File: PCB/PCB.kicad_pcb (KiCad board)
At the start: 2 copper layers, 60 x 70 mm, 6 parts

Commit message: update pcb
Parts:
- removed MD1, MD2: Conn_01x02_Pin, Connector_PinHeader_2.54mm:PinHeader_1x02_P2.54mm_Vertical
- removed MOTOR1, MOTOR2: Conn_01x09, Connector_PinHeader_2.54mm:PinHeader_1x09_P2.54mm_Vertical
- added D1: LED_RKGB, LED_THT:LED_D5.0mm-4_RGB_Wide_Pins, F.Cu at (86.7, 97.2)
- added J1: Servo_Conn_1, Connector_PinHeader_2.54mm:PinHeader_1x03_P2.54mm_Vertical, F.Cu at (64.5, 66.8)
- added J10: Conn_01x04_Pin, Connector_PinHeader_2.54mm:PinHeader_1x04_P2.54mm_Vertical, F.Cu at (82.8, 83.6)
- added J11: UBEC_Pow_In, Connector_PinHeader_2.54mm:PinHeader_1x02_P2.54mm_Horizontal, F.Cu at (78.2, 76.4)
- added J12: Spare_GPIO_Conn, Connector_PinHeader_2.54mm:PinHeader_1x10_P2.54mm_Vertical, F.Cu at (64.5, 76.4)
- added J2: Servo_Conn_2, Connector_PinHeader_2.54mm:PinHeader_1x03_P2.54mm_Vertical, F.Cu at (69.1, 66.8)
- added J3: Servo_Conn_3, Connector_PinHeader_2.54mm:PinHeader_1x03_P2.54mm_Vertical, F.Cu at (73.6, 66.8)
- added J4: Servo_Conn_4, Connector_PinHeader_2.54mm:PinHeader_1x03_P2.54mm_Vertical, F.Cu at (78.2, 66.8)
- added J5: Servo_Conn_5, Connector_PinHeader_2.54mm:PinHeader_1x03_P2.54mm_Vertical, F.Cu at (82.8, 66.8)
- added J6: Servo_Conn_6, Connector_PinHeader_2.54mm:PinHeader_1x03_P2.54mm_Vertical, F.Cu at (87.4, 66.8)
- added J7: Mot1_Conn, Connector_PinHeader_2.54mm:PinHeader_1x06_P2.54mm_Vertical, F.Cu at (69.1, 76.4)
- added J8: Mot2_Conn, Connector_PinHeader_2.54mm:PinHeader_1x06_P2.54mm_Vertical, F.Cu at (73.6, 76.4)
- added J9: Conn_01x04_Pin, Connector_PinHeader_2.54mm:PinHeader_1x04_P2.54mm_Vertical, F.Cu at (78.2, 83.6)
- added R1: 220R, Resistor_THT:R_Axial_DIN0207_L6.3mm_D2.5mm_P7.62mm_Horizontal, F.Cu at (86.7, 83.3)
- added R2: 220R, Resistor_THT:R_Axial_DIN0207_L6.3mm_D2.5mm_P7.62mm_Horizontal, F.Cu at (86.7, 87.3)
- added R3: 220R, Resistor_THT:R_Axial_DIN0207_L6.3mm_D2.5mm_P7.62mm_Horizontal, F.Cu at (86.7, 91.4)
- renumbered MOTOR_DRIVER1 to MOT_DRV_Conn1
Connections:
- net Net-(A2-GPIO21) renamed /PWM2
- A2 pad 1: unconnected-(A2-GPIO0-Pad1) -> /RED
- A2 pad 10: Net-(A2-GPIO7) -> /ENCA2
- A2 pad 11: Net-(A2-GPIO8) -> /GPIO8
- A2 pad 12: Net-(A2-GPIO9) -> /GPIO9
- A2 pad 13: Net-(MOTOR1-Pin_3) -> GND
- A2 pad 14: unconnected-(A2-GPIO10-Pad14) -> /GPIO10
- A2 pad 15: Net-(A2-GPIO11) -> /GPIO11
- A2 pad 16: Net-(A2-GPIO12) -> /GPIO12
- A2 pad 17: Net-(A2-GPIO13) -> /Srvo3_Sig
- A2 pad 18: Net-(MOTOR1-Pin_3) -> GND
- A2 pad 19: unconnected-(A2-GPIO14-Pad19) -> /Srvo2_Sig
- A2 pad 2: unconnected-(A2-GPIO1-Pad2) -> /GREEN
- A2 pad 20: unconnected-(A2-GPIO15-Pad20) -> /Srvo1_Sig
- A2 pad 21: Net-(A2-GPIO16) -> /PWM1
- A2 pad 22: Net-(A2-GPIO17) -> /INA1
- A2 pad 23: Net-(MOTOR1-Pin_3) -> GND
- A2 pad 24: Net-(A2-GPIO18) -> /INB1
- A2 pad 25: Net-(A2-GPIO19) -> /INB2
- A2 pad 26: unconnected-(A2-GPIO20-Pad26) -> /INA2
- A2 pad 28: Net-(MOTOR1-Pin_3) -> GND
- A2 pad 29: Net-(A2-GPIO22) -> /GPIO22
- A2 pad 3: Net-(MOTOR1-Pin_3) -> GND
- A2 pad 31: Net-(A2-GPIO26_ADC0) -> /ENCA1
- A2 pad 32: unconnected-(A2-GPIO27_ADC1-Pad32) -> /ENCB1
- A2 pad 33: unconnected-(A2-AGND-Pad33) -> GND
- A2 pad 34: unconnected-(A2-GPIO28_ADC2-Pad34) -> /GPIO28
- A2 pad 36: Net-(A2-3V3) -> +3V3
- A2 pad 38: Net-(MOTOR1-Pin_3) -> GND
- A2 pad 39: unconnected-(A2-VSYS-Pad39) -> 5VIN
- A2 pad 4: unconnected-(A2-GPIO2-Pad4) -> /BLUE
- A2 pad 40: Net-(A2-VBUS) -> VBUS
- A2 pad 5: unconnected-(A2-GPIO3-Pad5) -> /GPIO3
- A2 pad 6: unconnected-(A2-GPIO4-Pad6) -> /GPIO4
- A2 pad 7: unconnected-(A2-GPIO5-Pad7) -> /GPIO5
- A2 pad 8: Net-(MOTOR1-Pin_3) -> GND
- A2 pad 9: Net-(A2-GPIO6) -> /ENCB2
- MOT_DRV_Conn1 pad 1: Net-(MOTOR1-Pin_3) -> +3V3
- MOT_DRV_Conn1 pad 10: Net-(A2-3V3) -> GND
- MOT_DRV_Conn1 pad 2: Net-(MOTOR1-Pin_3) -> +3V3
- MOT_DRV_Conn1 pad 3: Net-(A2-GPIO13) -> /PWM1
- MOT_DRV_Conn1 pad 5: Net-(A2-GPIO12) -> /INA1
- MOT_DRV_Conn1 pad 6: Net-(A2-GPIO22) -> /INA2
- MOT_DRV_Conn1 pad 7: Net-(A2-GPIO11) -> /INB1
- MOT_DRV_Conn1 pad 8: Net-(A2-GPIO26_ADC0) -> /INB2
- MOT_DRV_Conn1 pad 9: Net-(A2-3V3) -> GND
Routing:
- net Net-(MOTOR1-Pin_3): track 107.4 -> 0.00 mm
- net Net-(A2-VBUS): track 100.9 -> 0.00 mm
- net Net-(A2-3V3): track 91.4 -> 0.00 mm
- net Net-(A2-GPIO26_ADC0): track 73.3 -> 0.00 mm
- net /PWM2: track 70.9 -> 0.00 mm
- net Net-(A2-GPIO22): track 70.1 -> 0.00 mm
- net Net-(A2-GPIO11): track 49.9 -> 0.00 mm
- net Net-(A2-GPIO12): track 46.3 -> 0.00 mm
- net Net-(A2-GPIO13): track 44.1 -> 0.00 mm
- net Net-(A2-GPIO8): track 11.0 -> 0.00 mm
- net Net-(A2-GPIO6): track 11.0 -> 0.00 mm
- net Net-(A2-GPIO7): track 11.0 -> 0.00 mm
- net Net-(A2-GPIO9): track 10.2 -> 0.00 mm
- net Net-(A2-GPIO16): track 9.70 -> 0.00 mm
- net Net-(A2-GPIO17): track 9.50 -> 0.00 mm
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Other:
- board outline removed
- copper layers 2 -> 4

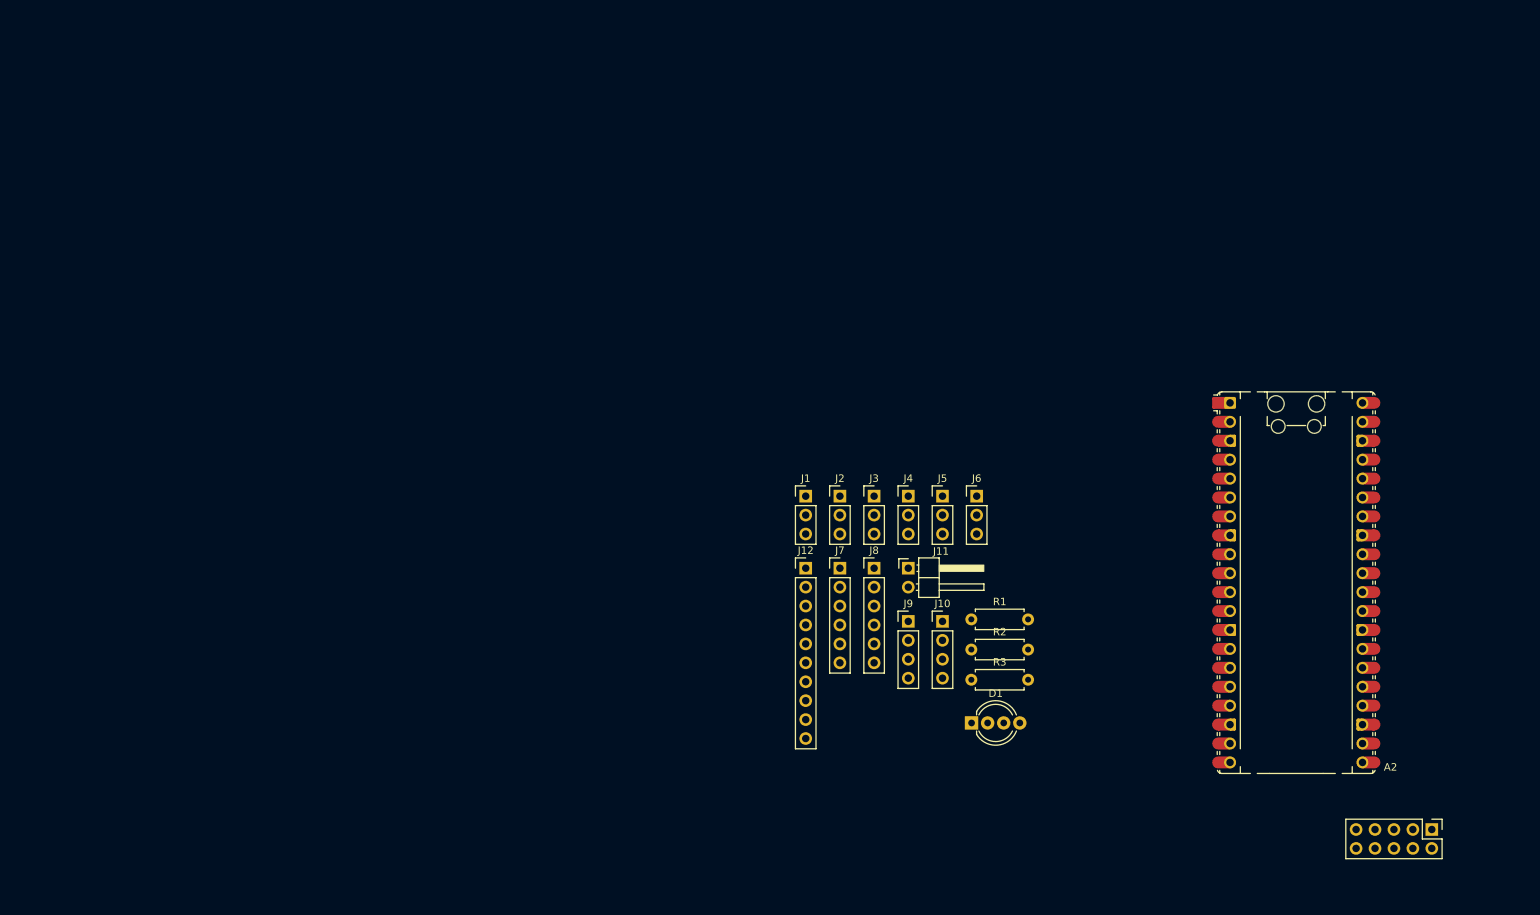
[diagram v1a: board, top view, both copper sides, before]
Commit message: update pico footprint
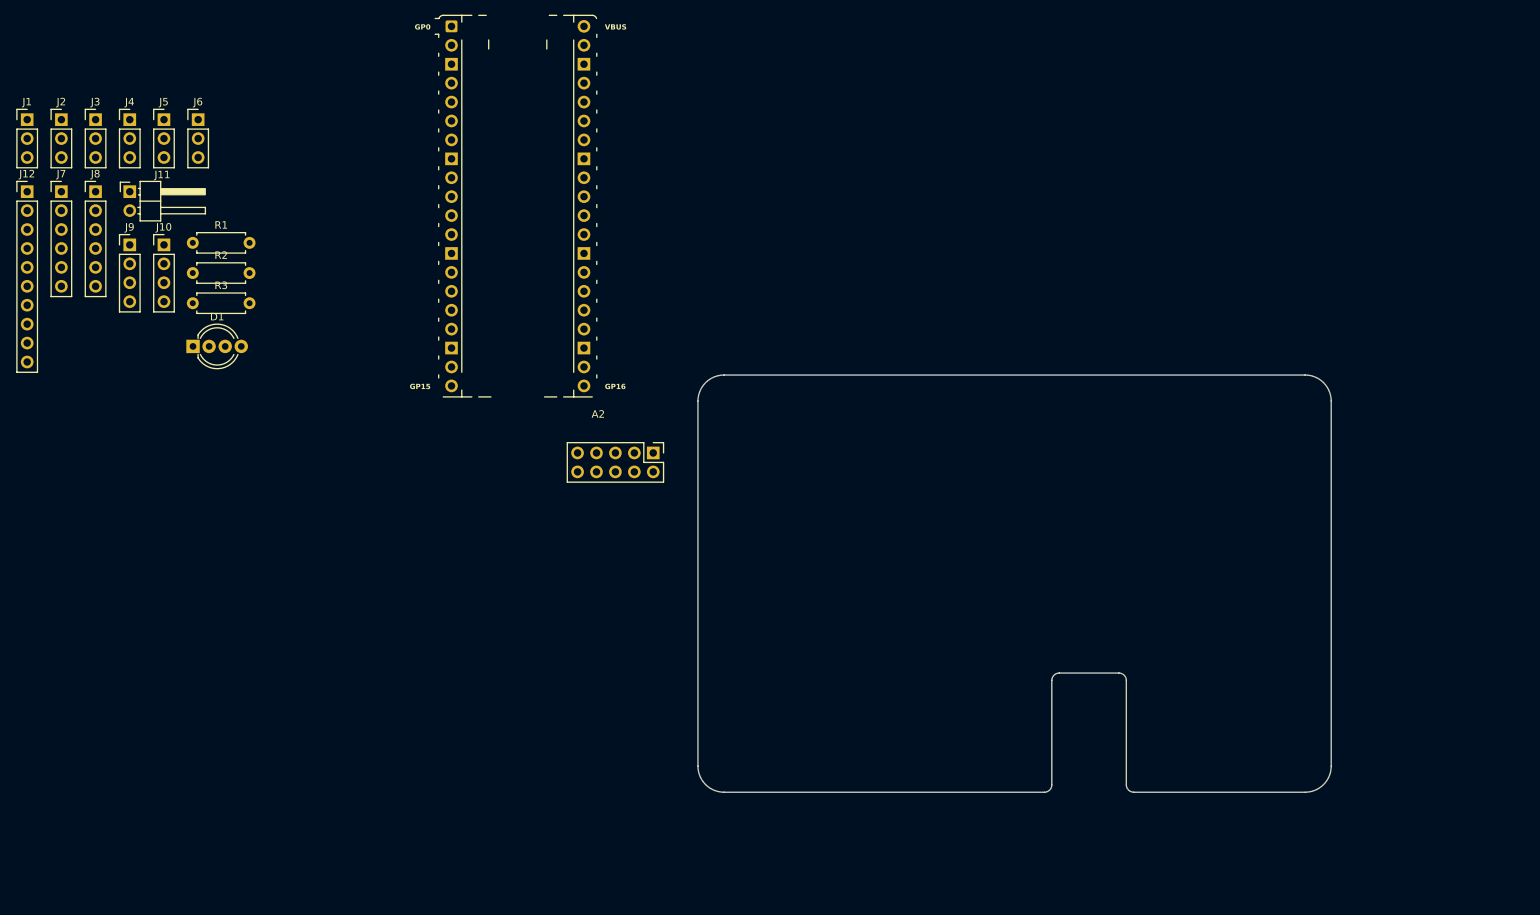
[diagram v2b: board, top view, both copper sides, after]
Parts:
- A2: footprint Module:RaspberryPi_Pico_Common_Unspecified -> RaspberryPi_Pico_THT:RaspberryPi_Pico_THT
- moved A2 116.1 mm to (25.8, 27.8)
- moved D1 116.1 mm to (-17.8, 46.7)
- moved J1 116.1 mm to (-40.0, 16.2)
- moved J10 116.1 mm to (-21.7, 33.0)
- moved J11 116.1 mm to (-26.3, 25.9)
- moved J12 116.1 mm to (-40.0, 25.9)
- moved J2 116.1 mm to (-35.4, 16.2)
- moved J3 116.1 mm to (-30.9, 16.2)
- moved J4 116.1 mm to (-26.3, 16.2)
- moved J5 116.1 mm to (-21.7, 16.2)
- moved J6 116.1 mm to (-17.1, 16.2)
- moved J7 116.1 mm to (-35.4, 25.9)
- moved J8 116.1 mm to (-30.9, 25.9)
- moved J9 116.1 mm to (-26.3, 33.0)
- moved MOT_DRV_Conn1 116.1 mm to (44.0, 61.0)
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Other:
- board outline added: 85 x 56 mm

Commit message: set mounting holes
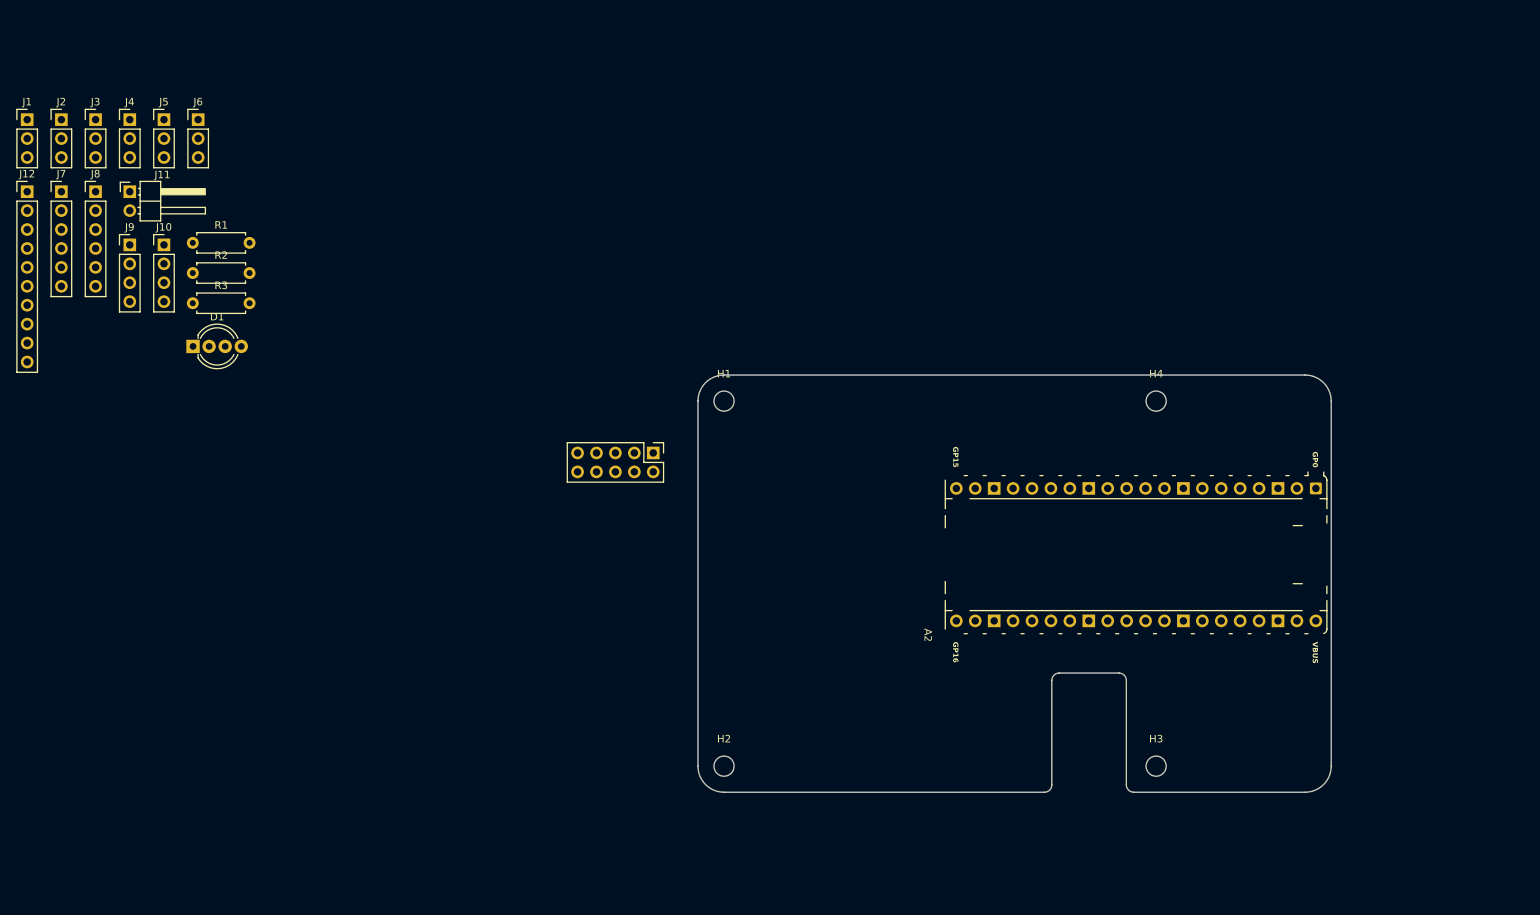
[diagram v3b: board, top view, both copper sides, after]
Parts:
- added H1: MountingHole_Pad, MountingHole:MountingHole_2.7mm_M2.5, F.Cu at (53.5, 54.0)
- added H2: MountingHole_Pad, MountingHole:MountingHole_2.7mm_M2.5, F.Cu at (53.5, 103.0)
- added H3: MountingHole_Pad, MountingHole:MountingHole_2.7mm_M2.5, F.Cu at (111.5, 103.0)
- added H4: MountingHole_Pad, MountingHole:MountingHole_2.7mm_M2.5, F.Cu at (111.5, 54.0)
- moved A2 95.3 mm to (108.8, 74.6), turned to -90 degrees

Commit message: update pcb layout
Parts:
- H1, H2, H3, H4: footprint MountingHole:MountingHole_2.7mm_M2.5 -> MountingHole:MountingHole_2.7mm_M2.5_Pad_Via
- J10: value Conn_01x04_Pin -> Mot2; footprint Connector_PinHeader_2.54mm:PinHeader_1x04_P2.54mm_Vertical -> Connector_PinHeader_2.54mm:PinHeader_2x02_P2.54mm_Vertical
- J11: value UBEC_Pow_In -> UBEC
- J9: value Conn_01x04_Pin -> Mot1; footprint Connector_PinHeader_2.54mm:PinHeader_1x04_P2.54mm_Vertical -> Connector_PinHeader_2.54mm:PinHeader_2x02_P2.54mm_Vertical
- moved J12 177.4 mm to (133.1, 64.5), turned to -90 degrees
- moved J7 172.1 mm to (117.9, 104.0), turned to 90 degrees
- moved J9 158.5 mm to (117.9, 98.9), turned to 90 degrees
- moved D1 151.7 mm to (125.5, 96.3)
- moved J8 151.2 mm to (117.9, 53.0), turned to 90 degrees
- moved R1 144.2 mm to (118.4, 80.1)
- moved J10 142.3 mm to (117.9, 60.7), turned to 90 degrees
- moved R2 142.0 mm to (118.4, 76.9)
- moved R3 140.1 mm to (118.4, 73.7)
- moved J11 134.6 mm to (102.7, 64.5), turned to 90 degrees
- moved S1 133.9 mm to (84.9, 64.5), turned to 180 degrees
- moved J4 132.9 mm to (97.6, 64.5), turned to 180 degrees
- moved S2 132.0 mm to (87.4, 64.5), turned to 180 degrees
- moved S3 130.1 mm to (90.0, 64.5), turned to 180 degrees
- moved J5 126.3 mm to (95.0, 64.5), turned to 180 degrees
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- renumbered J1 to S1, J2 to S2, J3 to S3
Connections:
- MOT_DRV_Conn1 pad 3: /PWM1 -> /PWM2
- MOT_DRV_Conn1 pad 4: /PWM2 -> /PWM1
- MOT_DRV_Conn1 pad 5: /INA1 -> /INA2
- MOT_DRV_Conn1 pad 6: /INA2 -> /INA1
- MOT_DRV_Conn1 pad 7: /INB1 -> /INB2
- MOT_DRV_Conn1 pad 8: /INB2 -> /INB1
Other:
- outline, holes or cut-outs redrawn
- board text added: "3V3"
- board text added: "A1"
- board text added: "A2"
- board text added: "B1"
- board text added: "B2"
- board text added: "BLK"
- board text added: "DFR0601"
- board text added: "EC1"
- board text added: "EC2"
- board text added: "GND"
- board text added: "GP10"
- board text added: "GP11"
- board text added: "GP12"
- board text added: "GP4"
- board text added: "GP5"
- board text added: "GP8"
- board text added: "GP9"
- board text added: "P1"
- board text added: "P2"
- board text added: "RED"
- board text added: "VBU"

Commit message: pour copper to GND
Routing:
- added copper zone on B.Cu, net GND
- added copper zone on F.Cu, net GND
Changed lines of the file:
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@@
 			)
 			(rotate
-				(xyz 0 0 0)
+				(xyz -0 -0 -0)
 			)
 		)
@@
 		)
 	)
+	(zone
+		(net 2)
+		(net_name "GND")
+		(layers "F.Cu" "B.Cu")
+		(hatch edge 0.5)
+		(connect_pads
+			(clearance 0.5)
+		)
+		(min_thickness 0.25)
+		(filled_areas_thickness no)
+		(fill yes
+			(thermal_gap 0.5)
+			(thermal_bridge_width 0.5)
+		)
+		(polygon
+			(pts
+				(xy 43.3 45) (xy 41.15 117.3) (xy 144.95 118.55) (xy 140.35 44.7) (xy 43.3 44.9) (xy 43.95 44.9)
+				(xy 43.4 45.1)
+			)
+		)
+	)

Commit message: wire up
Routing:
- net VBUS: track 0.00 -> 66.1 mm, vias 0 -> 2
- net +3V3: track 0.00 -> 45.8 mm
- net Net-(D1-BA): track 0.00 -> 28.3 mm
- net /ENCA2: track 0.00 -> 28.2 mm
- net /ENCA1: track 0.00 -> 26.6 mm
- net /ENCB2: track 0.00 -> 26.6 mm
- net /ENCB1: track 0.00 -> 26.0 mm
- net Net-(D1-GA): track 0.00 -> 24.2 mm
- net /GPIO12: track 0.00 -> 20.1 mm, vias 0 -> 1
- net Net-(D1-RA): track 0.00 -> 19.2 mm
- net +6V: track 0.00 -> 18.8 mm
- net /GPIO9: track 0.00 -> 17.3 mm
- net /GPIO11: track 0.00 -> 17.3 mm
- net /GPIO8: track 0.00 -> 17.3 mm
- net /GPIO10: track 0.00 -> 17.3 mm
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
